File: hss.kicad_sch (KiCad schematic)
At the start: 4 parts, among them U1 TPS1H100AQPWPRQ1

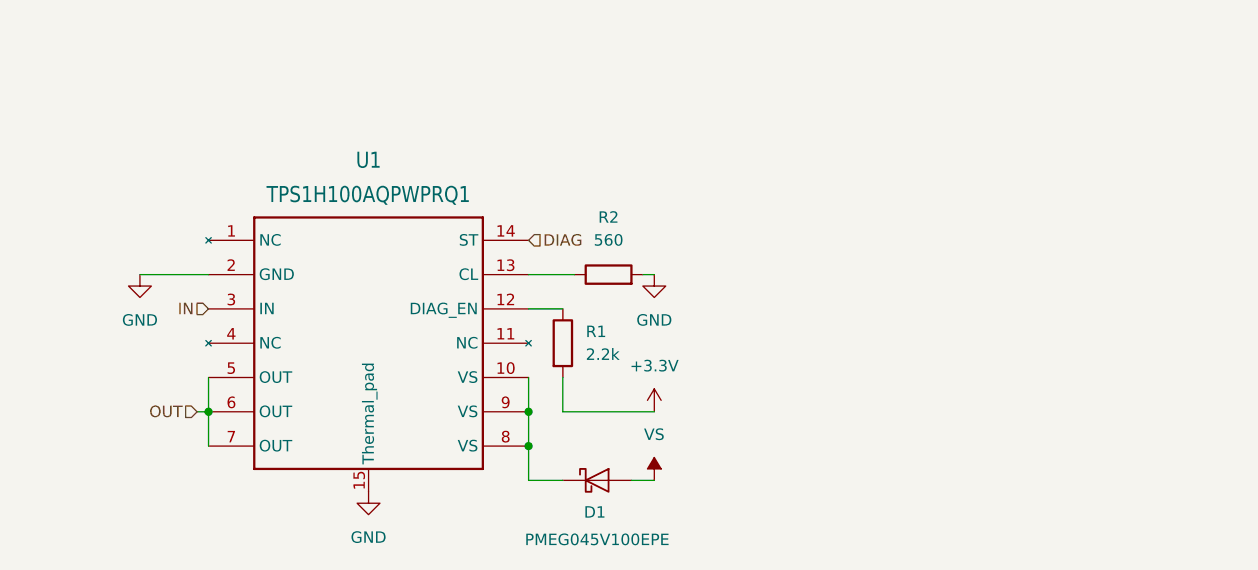
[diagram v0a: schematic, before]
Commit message: Switch to TPS27S100A, replace series diodes with GND network
- U1-U4: TPS27S100APWPR (pin-compatible; TPS1H100A had 11 in stock at
  JLCPCB). Existing footprint is already the TPS27S100 one.
- Remove the PMEG045 series diodes (1.09 USD each, ~2 W loss at 4 A).
  Reverse polarity is handled by the datasheet GND network instead:
  1k || DSK16 from device GND (DGND) to board GND; ILIM resistor and
  thermal pad moved to DGND as the datasheet requires.
- 4.7k series resistors on EN and FLT (datasheet: >= 4.7k on I/O pins).
- 10k FLT pull-up to 3.3 V now lives on the module.
- DIAG_EN pull-up 2.2k -> 4.7k.
- Note: header pin 12 (GND) = MOD_ID 0 for the base board.

ERC unchanged (15 pre-existing power-flag warnings).

Co-Authored-By: Claude Opus 5.5 <noreply@anthropic.com>
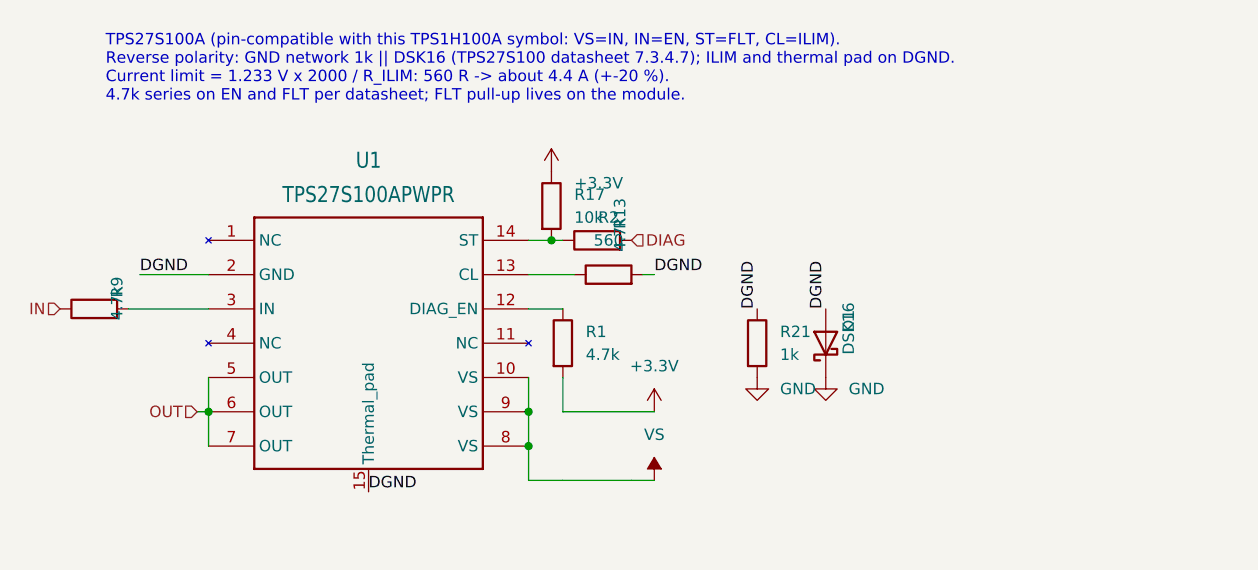
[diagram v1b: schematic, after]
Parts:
- removed D1: PMEG045V100EPE, Package_TO_SOT_SMD:TO-277A, symbol Diode:PMEG045T100EPD
- added D1: DSK16, Diode_SMD:D_SOD-123F, symbol Device:D_Schottky
- added R13, R9: 4.7k, Resistor_SMD:R_0402_1005Metric, symbol Device:R
- added R17: 10k, Resistor_SMD:R_0402_1005Metric, symbol Device:R
- added R21: 1k, Resistor_SMD:R_0402_1005Metric, symbol Device:R
- R1: value 2.2k -> 4.7k; LCSC (none) -> C25900
- U1: value TPS1H100AQPWPRQ1 -> TPS27S100APWPR; LCSC (none) -> C2879389
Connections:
- net +3.3V: now also R17.1
- net DIAG: now also R13.2; no longer U1.14 (ST)
- net GND: now also D1.1 (K), R21.2; no longer R2.2, U1.15 (Thermal_pad), U1.2 (GND)
- net IN: now also R9.1; no longer U1.3 (IN)
- net VS: now also U1.10 (VS), U1.8 (VS), U1.9 (VS)
- new net: R9.2, U1.3 (IN)
- new net: R13.1, R17.2, U1.14 (ST)
- new net DGND: D1.2 (A), R2.2, R21.1, U1.15 (Thermal_pad), U1.2 (GND)
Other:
- note added: "TPS27S100A (pin-compatible with this TPS1H100A symbol: VS=IN, IN=EN, ST=FLT, CL=ILIM). Reverse polarity: GND network 1k || DSK16 (TPS27S100 datasheet 7.3.4.7); ILIM and thermal pad on DGND. Current limit = 1.233 V x 2000 / R_ILIM: 560 R -> about 4.4 A (+-20 %). 4.7k series on EN and FLT per datasheet; FLT pull-up lives on the module."

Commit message: Add surge clamp on VS, basic ILIM resistor, clean up ERC
- D5: SMCJ30CA (1.5 kW bidirectional) across VS-GND at the module power
  input. TPS27S100 is 40 V max (48 V < 400 ms); clamp is 48.4 V at 31 A
  and lower at smaller surge currents. Bidirectional so a reversed
  battery is not shorted.
- ILIM resistors 560 R moved to 0603 (basic part C23204).
- ERC: TPS1H100A symbol OUT pins 6/7 passive (paralleled outputs);
  PWR_FLAGs on VS, GND, +3.3V and per-channel DGND.

ERC: 0 violations.

Co-Authored-By: Claude Opus 5.5 <noreply@anthropic.com>
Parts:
- R2: footprint Resistor_SMD:R_0402_1005Metric -> Resistor_SMD:R_0603_1608Metric; LCSC (none) -> C23204
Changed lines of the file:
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@@
 			)
 		)
-		(property "Footprint" "Resistor_SMD:R_0402_1005Metric"
+		(property "Footprint" "Resistor_SMD:R_0603_1608Metric"
 			(at 156.21 75.438 90)
 			(effects
@@
 		)
 		(property "Description" "Resistor"
+			(at 156.21 73.66 0)
+			(effects
+				(font
+					(size 1.27 1.27)
+				)
+				(hide yes)
+			)
+		)
+		(property "LCSC" "C23204"
 			(at 156.21 73.66 0)
 			(effects
@@
 		)
 	)
+	(symbol
+		(lib_id "power:PWR_FLAG")
+		(at 172.72 77.47 0)
+		(unit 1)
+		(exclude_from_sim no)
+		(in_bom no)
+		(on_board yes)
+		(dnp no)
+		(fields_autoplaced yes)
+		(property "Reference" "#FLG01"
+			(at 175.26 76.2 0)
+			(effects
+				(font
+					(size 1.27 1.27)
+				)
+				(hide yes)
+			)
+		)
+		(property "Value" "PWR_FLAG"
+			(at 175.26 78.74 0)
+			(effects
+				(font
+					(size 1.27 1.27)
+				)
+				(justify left)
+			)
+		)
+		(property "Footprint" ""
+			(at 172.72 77.47 0)
+			(effects
+				(font
+					(size 1.27 1.27)
+				)
+				(hide yes)
+			)
+		)
+		(property "Datasheet" "~"
+			(at 172.72 77.47 0)
+			(effects
+				(font
+					(size 1.27 1.27)
+				)
+				(hide yes)
+			)
+		)
+		(property "Description" "Special symbol for telling ERC where power comes from"
+			(at 172.72 77.47 0)
+			(effects
+				(font
+					(size 1.27 1.27)
+				)
+				(hide yes)
+			)
+		)
+		(pin "1"
+		)
+		(instances
+			(project "ESP32-PDM"
+				(path "/77f0f044-4c8a-4320-9763-77a575781bec/320a4353-39e5-4d3f-bddd-b8f5d4b99b21"
+					(reference "#FLG01")
+					(unit 1)
+				)
+				(path "/77f0f044-4c8a-4320-9763-77a575781bec/b3141720-4b20-4c55-afb4-4c446b42fccb"
+					(reference "#FLG02")
+					(unit 1)
+				)
+				(path "/77f0f044-4c8a-4320-9763-77a575781bec/cda3d90b-a08e-41ae-9565-1f9302b4b7b5"
+					(reference "#FLG03")
+					(unit 1)
+				)
+				(path "/77f0f044-4c8a-4320-9763-77a575781bec/df741068-1b51-4579-a9e1-d1030dd5ba08"
+					(reference "#FLG04")
+					(unit 1)
+				)
+			)
+		)
+	)

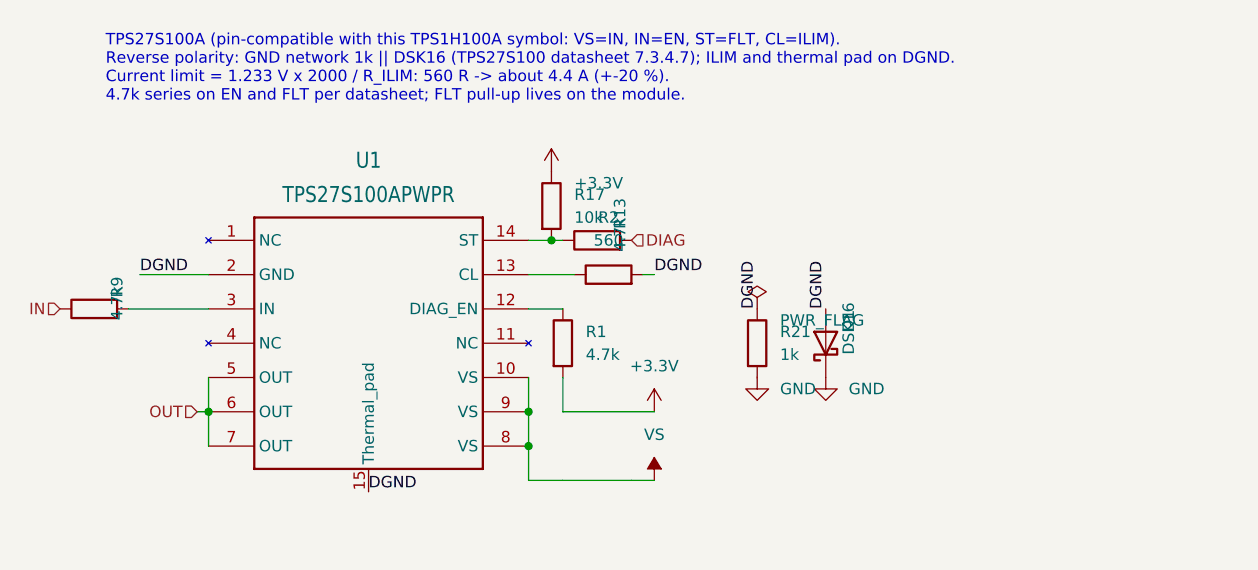
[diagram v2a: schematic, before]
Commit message: Use TPS27S100B with current monitor on DIAG lines
- U1-U4: TPS27S100BPWPR (IMON current-sense output, 1.85 USD vs 2.02).
- R17-R20: FLT pull-up becomes the 330 R IMON resistor to board GND:
  I_load/500 into 330 R || 14.7k -> ~0.65 V/A, linear to 4 V.
- New R25-R28 10k to GND after the 4.7k series: header DIAG = 0.68 x
  IMON (~0.44 V/A; fault level 4.3-4.9 V -> 2.9-3.3 V, below the
  ESP32 3.6 V abs max). Base reads it on ADC1 (IO2-IO5).

ERC: 0 violations.

Co-Authored-By: Claude Opus 5.5 <noreply@anthropic.com>
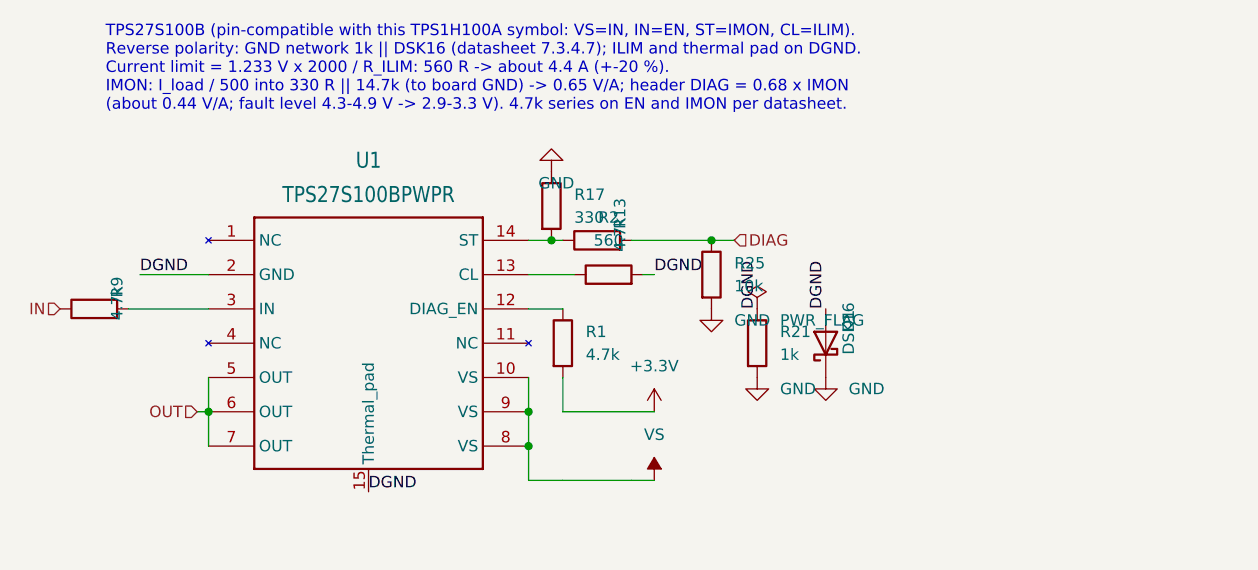
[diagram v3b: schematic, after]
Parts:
- added R25: 10k, Resistor_SMD:R_0402_1005Metric, symbol Device:R
- R17: value 10k -> 330; LCSC C25744 -> C25104
- U1: value TPS27S100APWPR -> TPS27S100BPWPR; LCSC C2879389 -> C2680365
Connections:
- net +3.3V: no longer R17.1
- net DIAG: now also R25.1
- net GND: now also R17.1, R25.2
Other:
- note added: "TPS27S100B (pin-compatible with this TPS1H100A symbol: VS=IN, IN=EN, ST=IMON, CL=ILIM). Reverse polarity: GND network 1k || DSK16 (datasheet 7.3.4.7); ILIM and thermal pad on DGND. Current limit = 1.233 V x 2000 / R_ILIM: 560 R -> about 4.4 A (+-20 %). IMON: I_load / 500 into 330 R || 14.7k (to board GND) -> 0.65 V/A; header DIAG = 0.68 x IMON (about 0.44 V/A; fault level 4.3-4.9 V -> 2.9-3.3 V).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"
- note removed: "TPS27S100A (pin-compatible with this TPS1H100A symbol: VS=IN, IN=EN, ST=FLT, CL=ILIM). Reverse polarity: GND network 1k || DSK16 (TPS27S100 datasheet 7.3.4.7); ILIM and thermal pad on DGND. Current limit = 1.233 V x 2000 / R_ILIM: 560 R -> about 4.4 A (+-20 %). 4.7k series on EN and FLT per datasheet; FLT pull-up lives on the module."
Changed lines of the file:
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@@
 	(hierarchical_label "DIAG"
 		(shape input)
-		(at 158.75 69.85 0)
+		(at 170.18 69.85 0)
 		(effects
 			(font
@@
 			)
 		)
-		(property "Value" "TPS27S100APWPR"
+		(property "Value" "TPS27S100BPWPR"
 			(at 129.54 64.77 0)
 			(effects
@@
 			)
 		)
-		(property "LCSC" "C2879389"
+		(property "LCSC" "C2680365"
 			(at 129.54 90.17 0)
 			(effects
@@
 			)
 		)
-		(property "Value" "10k"
+		(property "Value" "330"
 			(at 152.4 67.31 0)
 			(effects
@@
 			)
 		)
-		(property "LCSC" "C25744"
+		(property "LCSC" "C25104"
 			(at 149.86 66.04 0)
 			(effects
@@
 		)
 	)
-	(symbol
-		(lib_id "power:+3.3V")
-		(at 149.86 62.23 0)
-		(unit 1)
-		(exclude_from_sim no)
-		(in_bom no)
-		(on_board yes)
-		(dnp no)
-		(fields_autoplaced yes)
-		(property "Reference" "#PWR038"
-			(at 152.4 60.96 0)
-			(effects
-				(font
-					(size 1.27 1.27)
-				)
-				(hide yes)
-			)
-		)
-		(property "Value" "+3.3V"
-			(at 152.4 63.5 0)
-			(effects
-				(font
-					(size 1.27 1.27)
-				)
-				(justify left)
-			)
-		)
-		(property "Footprint" ""
-			(at 149.86 62.23 0)
-			(effects
-				(font
-					(size 1.27 1.27)
-				)
-				(hide yes)
-			)
-		)
-		(property "Datasheet" ""
-			(at 149.86 62.23 0)
-			(effects
-				(font
-					(size 1.27 1.27)
-				)
-				(hide yes)
-			)
-		)
-		(property "Description" "Power symbol creates a global label with name \"+3.3V\""
-			(at 149.86 62.23 0)
-			(effects
-				(font
-					(size 1.27 1.27)
-				)
-				(hide yes)
-			)
-		)
-		(pin "1"
-		)
-		(instances
-			(project "ESP32-PDM"
-				(path "/77f0f044-4c8a-4320-9763-77a575781bec/320a4353-39e5-4d3f-bddd-b8f5d4b99b21"
-					(reference "#PWR038")
-					(unit 1)
-				)
-				(path "/77f0f044-4c8a-4320-9763-77a575781bec/b3141720-4b20-4c55-afb4-4c446b42fccb"
-					(reference "#PWR039")
-					(unit 1)
-				)
-				(path "/77f0f044-4c8a-4320-9763-77a575781bec/df741068-1b51-4579-a9e1-d1030dd5ba08"
-					(reference "#PWR040")
-					(unit 1)
-				)
-				(path "/77f0f044-4c8a-4320-9763-77a575781bec/cda3d90b-a08e-41ae-9565-1f9302b4b7b5"
-					(reference "#PWR041")
-					(unit 1)
-				)
-			)
-		)
-	)
-	(text "TPS27S100A (pin-compatible with this TPS1H100A symbol: VS=IN, IN=EN, ST=FLT, CL=ILIM).\nReverse polarity: GND network 1k || DSK16 (TPS27S100 datasheet 7.3.4.7); ILIM and thermal pad on DGND.\nCurrent limit = 1.233 V x 2000 / R_ILIM: 560 R -> about 4.4 A (+-20 %).\n4.7k series on EN and FLT per datasheet; FLT pull-up lives on the module."
+	(text "TPS27S100B (pin-compatible with this TPS1H100A symbol: VS=IN, IN=EN, ST=IMON, CL=ILIM).\nReverse polarity: GND network 1k || DSK16 (datasheet 7.3.4.7); ILIM and thermal pad on DGND.\nCurrent limit = 1.233 V x 2000 / R_ILIM: 560 R -> about 4.4 A (+-20 %).\nIMON: I_load / 500 into 330 R || 14.7k (to board GND) -> 0.65 V/A; header DIAG = 0.68 x IMON\n(about 0.44 V/A; fault level 4.3-4.9 V -> 2.9-3.3 V). 4.7k series on EN and IMON per datasheet."
 		(exclude_from_sim no)
 		(at 100.33 50.8 0)
@@
 					(unit 1)
 				)
+			)
+		)
+	)
+	(symbol
+		(lib_id "power:GND")
+		(at 149.86 62.23 180)
+		(unit 1)
+		(exclude_from_sim no)
+		(in_bom no)
+		(on_board yes)
+		(dnp no)
+		(fields_autoplaced yes)
+		(property "Reference" "#PWR045"
+			(at 152.4 60.96 0)
+			(effects
+				(font
+					(size 1.27 1.27)
+				)
+				(hide yes)
+			)
+		)
+		(property "Value" "GND"
+			(at 152.4 63.5 0)
+			(effects
+				(font
+					(size 1.27 1.27)
+				)
+				(justify left)
+			)
+		)
+		(property "Footprint" ""
+			(at 149.86 62.23 0)
+			(effects
+				(font
+					(size 1.27 1.27)
+				)
+				(hide yes)
+			)
+		)
+		(property "Datasheet" ""
+			(at 149.86 62.23 0)
+			(effects
+				(font
+					(size 1.27 1.27)
+				)
+				(hide yes)
+			)
+		)
+		(property "Description" "Power symbol creates a global label with name \"GND\" , ground"
+			(at 149.86 62.23 0)
+			(effects
+				(font
+					(size 1.27 1.27)
+				)
+				(hide yes)
+			)
+		)
+		(pin "1"
+		)
+		(instances
+			(project "ESP32-PDM"
+				(path "/77f0f044-4c8a-4320-9763-77a575781bec/320a4353-39e5-4d3f-bddd-b8f5d4b99b21"
+					(reference "#PWR045")
+					(unit 1)
+				)
+				(path "/77f0f044-4c8a-4320-9763-77a575781bec/b3141720-4b20-4c55-afb4-4c446b42fccb"
+					(reference "#PWR046")
+					(unit 1)
+				)
+				(path "/77f0f044-4c8a-4320-9763-77a575781bec/cda3d90b-a08e-41ae-9565-1f9302b4b7b5"
+					(reference "#PWR047")
+					(unit 1)
+				)
+				(path "/77f0f044-4c8a-4320-9763-77a575781bec/df741068-1b51-4579-a9e1-d1030dd5ba08"
+					(reference "#PWR048")
+					(unit 1)
+				)
+			)
+		)
+	)
+	(wire
+		(pts
+			(xy 158.75 69.85)
+			(xy 167.64 69.85)
+		)
+		(stroke
+			(width 0)
+			(type default)
+		)
+	)
+	(wire
+		(pts
+			(xy 167.64 69.85)
+			(xy 170.18 69.85)
+		)
+		(stroke
+			(width 0)
+			(type default)
+		)
+	)
+	(junction
+		(at 167.64 69.85)
+		(diameter 0)
+		(color 0 0 0 0)
+	)
+	(symbol
+		(lib_id "Device:R")
+		(at 167.64 73.66 0)
+		(unit 1)
+		(exclude_from_sim no)
+		(in_bom yes)
+		(on_board yes)
+		(dnp no)
+		(fields_autoplaced yes)
+		(property "Reference" "R25"
+			(at 170.18 72.39 0)
+			(effects
+				(font
+					(size 1.27 1.27)
+				)
+				(justify left)
+			)
+		)
+		(property "Value" "10k"
+			(at 170.18 74.93 0)
+			(effects
+				(font
+					(size 1.27 1.27)
+				)
+				(justify left)
+			)
+		)
+		(property "Footprint" "Resistor_SMD:R_0402_1005Metric"
+			(at 167.64 73.66 0)
+			(effects
+				(font
+					(size 1.27 1.27)
+				)
+				(hide yes)
+			)
+		)
+		(property "Datasheet" "~"
+			(at 167.64 73.66 0)
+			(effects
+				(font
+					(size 1.27 1.27)
+				)
+				(hide yes)
+			)
+		)
+		(property "Description" "Resistor"
+			(at 167.64 73.66 0)
+			(effects
+				(font
+					(size 1.27 1.27)
+				)
+				(hide yes)
+			)
+		)
+		(property "LCSC" "C25744"
+			(at 167.64 73.66 0)
+			(effects
+				(font
+					(size 1.27 1.27)
+				)
+				(hide yes)
+			)
+		)
+		(pin "1"
+		)
+		(pin "2"
+		)
+		(instances
+			(project "ESP32-PDM"
+				(path "/77f0f044-4c8a-4320-9763-77a575781bec/320a4353-39e5-4d3f-bddd-b8f5d4b99b21"
+					(reference "R25")
+					(unit 1)
+				)
+				(path "/77f0f044-4c8a-4320-9763-77a575781bec/b3141720-4b20-4c55-afb4-4c446b42fccb"
+					(reference "R26")
+					(unit 1)
+				)
+				(path "/77f0f044-4c8a-4320-9763-77a575781bec/cda3d90b-a08e-41ae-9565-1f9302b4b7b5"
+					(reference "R27")
+					(unit 1)
+				)
+				(path "/77f0f044-4c8a-4320-9763-77a575781bec/df741068-1b51-4579-a9e1-d1030dd5ba08"
+					(reference "R28")
+					(unit 1)
+				)
+			)
+		)
+	)
+	(symbol
+		(lib_id "power:GND")
+		(at 167.64 77.47 0)
+		(unit 1)
+		(exclude_from_sim no)
+		(in_bom no)
+		(on_board yes)
+		(dnp no)
+		(fields_autoplaced yes)
+		(property "Reference" "#PWR049"
+			(at 170.18 76.2 0)
+			(effects
+				(font
+					(size 1.27 1.27)
+				)
+				(hide yes)
+			)
+		)
+		(property "Value" "GND"
+			(at 170.18 78.74 0)
+			(effects
+				(font
+					(size 1.27 1.27)
+				)
+				(justify left)
+			)
+		)
+		(property "Footprint" ""
+			(at 167.64 77.47 0)
+			(effects
+				(font
+					(size 1.27 1.27)
+				)
+				(hide yes)
+			)
+		)
+		(property "Datasheet" ""
+			(at 167.64 77.47 0)
+			(effects
+				(font
+					(size 1.27 1.27)
+				)
+				(hide yes)
+			)
+		)
+		(property "Description" "Power symbol creates a global label with name \"GND\" , ground"
+			(at 167.64 77.47 0)
+			(effects
+				(font
+					(size 1.27 1.27)
+				)
+				(hide yes)
+			)
+		)
+		(pin "1"
+		)
+		(instances
+			(project "ESP32-PDM"
+				(path "/77f0f044-4c8a-4320-9763-77a575781bec/320a4353-39e5-4d3f-bddd-b8f5d4b99b21"
+					(reference "#PWR049")
+					(unit 1)
+				)
+				(path "/77f0f044-4c8a-4320-9763-77a575781bec/b3141720-4b20-4c55-afb4-4c446b42fccb"
+					(reference "#PWR050")
+					(unit 1)
+				)
+				(path "/77f0f044-4c8a-4320-9763-77a575781bec/cda3d90b-a08e-41ae-9565-1f9302b4b7b5"
+					(reference "#PWR051")
+					(unit 1)
+				)
+				(path "/77f0f044-4c8a-4320-9763-77a575781bec/df741068-1b51-4579-a9e1-d1030dd5ba08"
+					(reference "#PWR052")
+					(unit 1)
+				)
